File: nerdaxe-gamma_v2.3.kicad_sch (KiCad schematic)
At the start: 20 parts, among them J1 54-00164

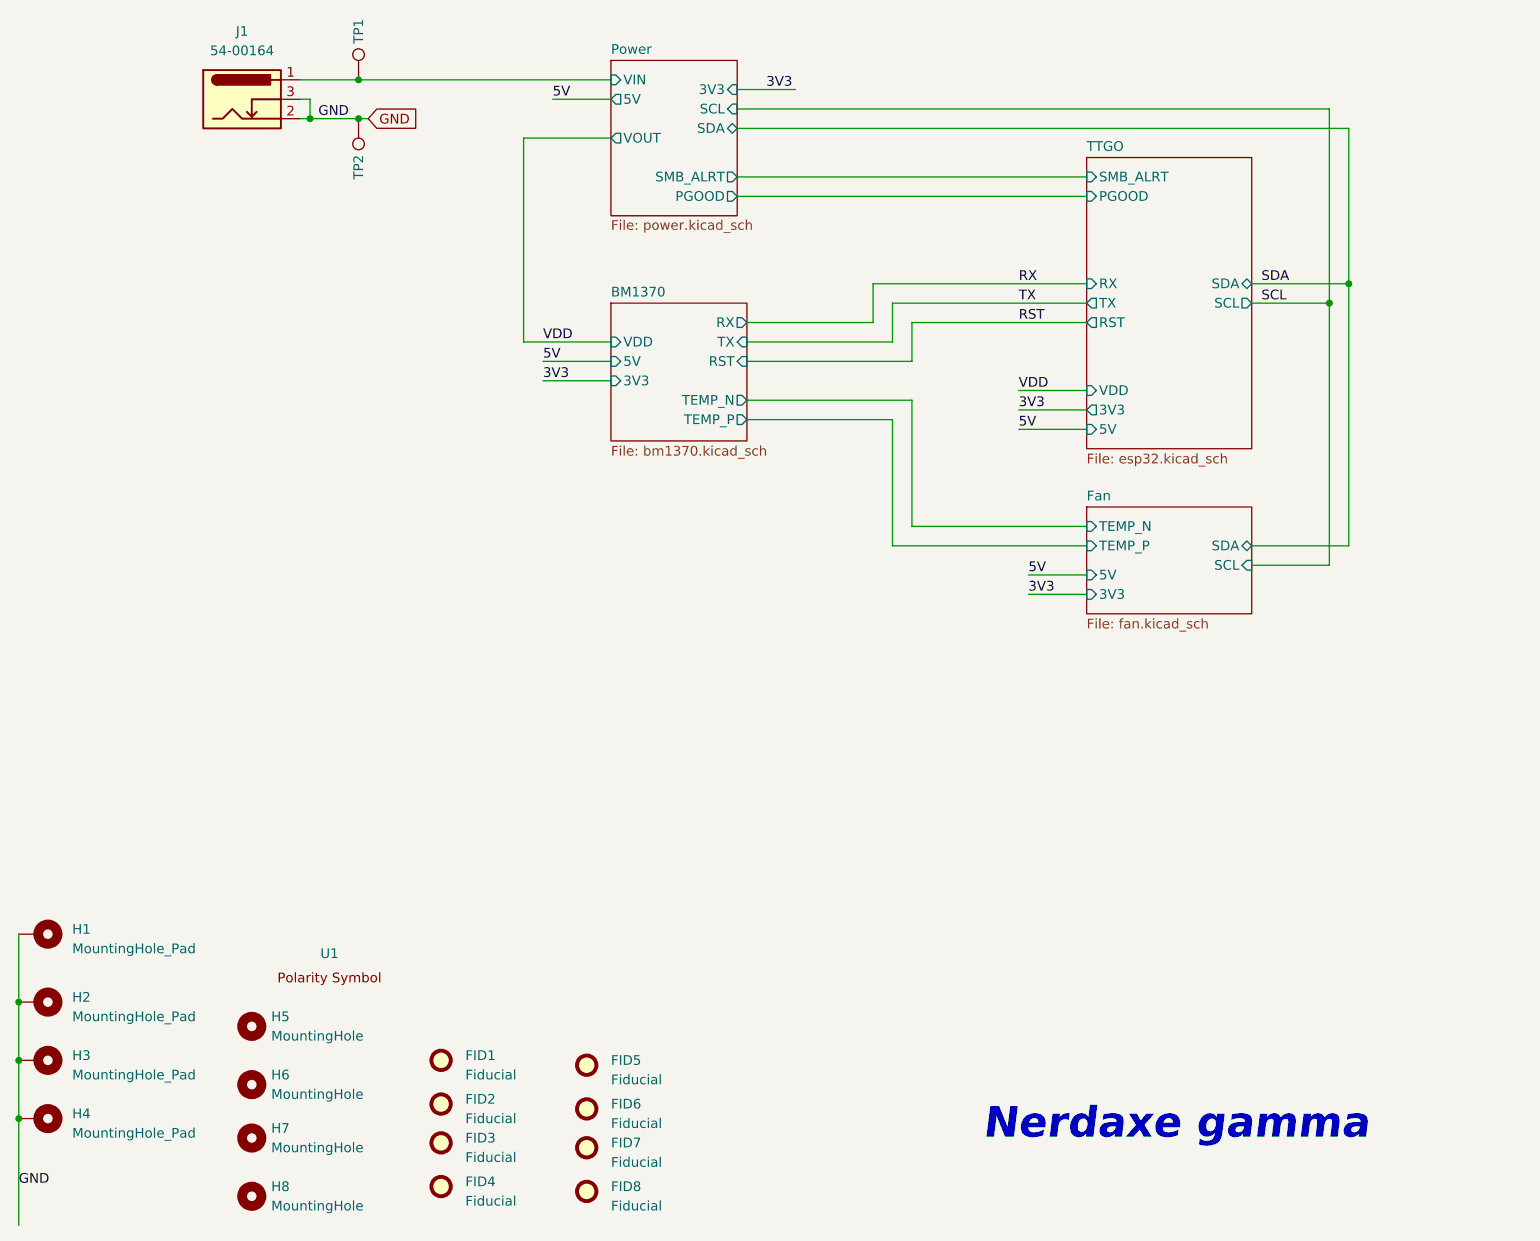
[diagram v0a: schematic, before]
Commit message: Nerdaxe Gamma v2.3
- Fix Emi CE needs
- Added ferrite beads + EMI blocking capacitors
- New components added: R16, R20, R26, R27C21, C22, C23, FB1, FB2, FB3, FB4, FB5, FB6
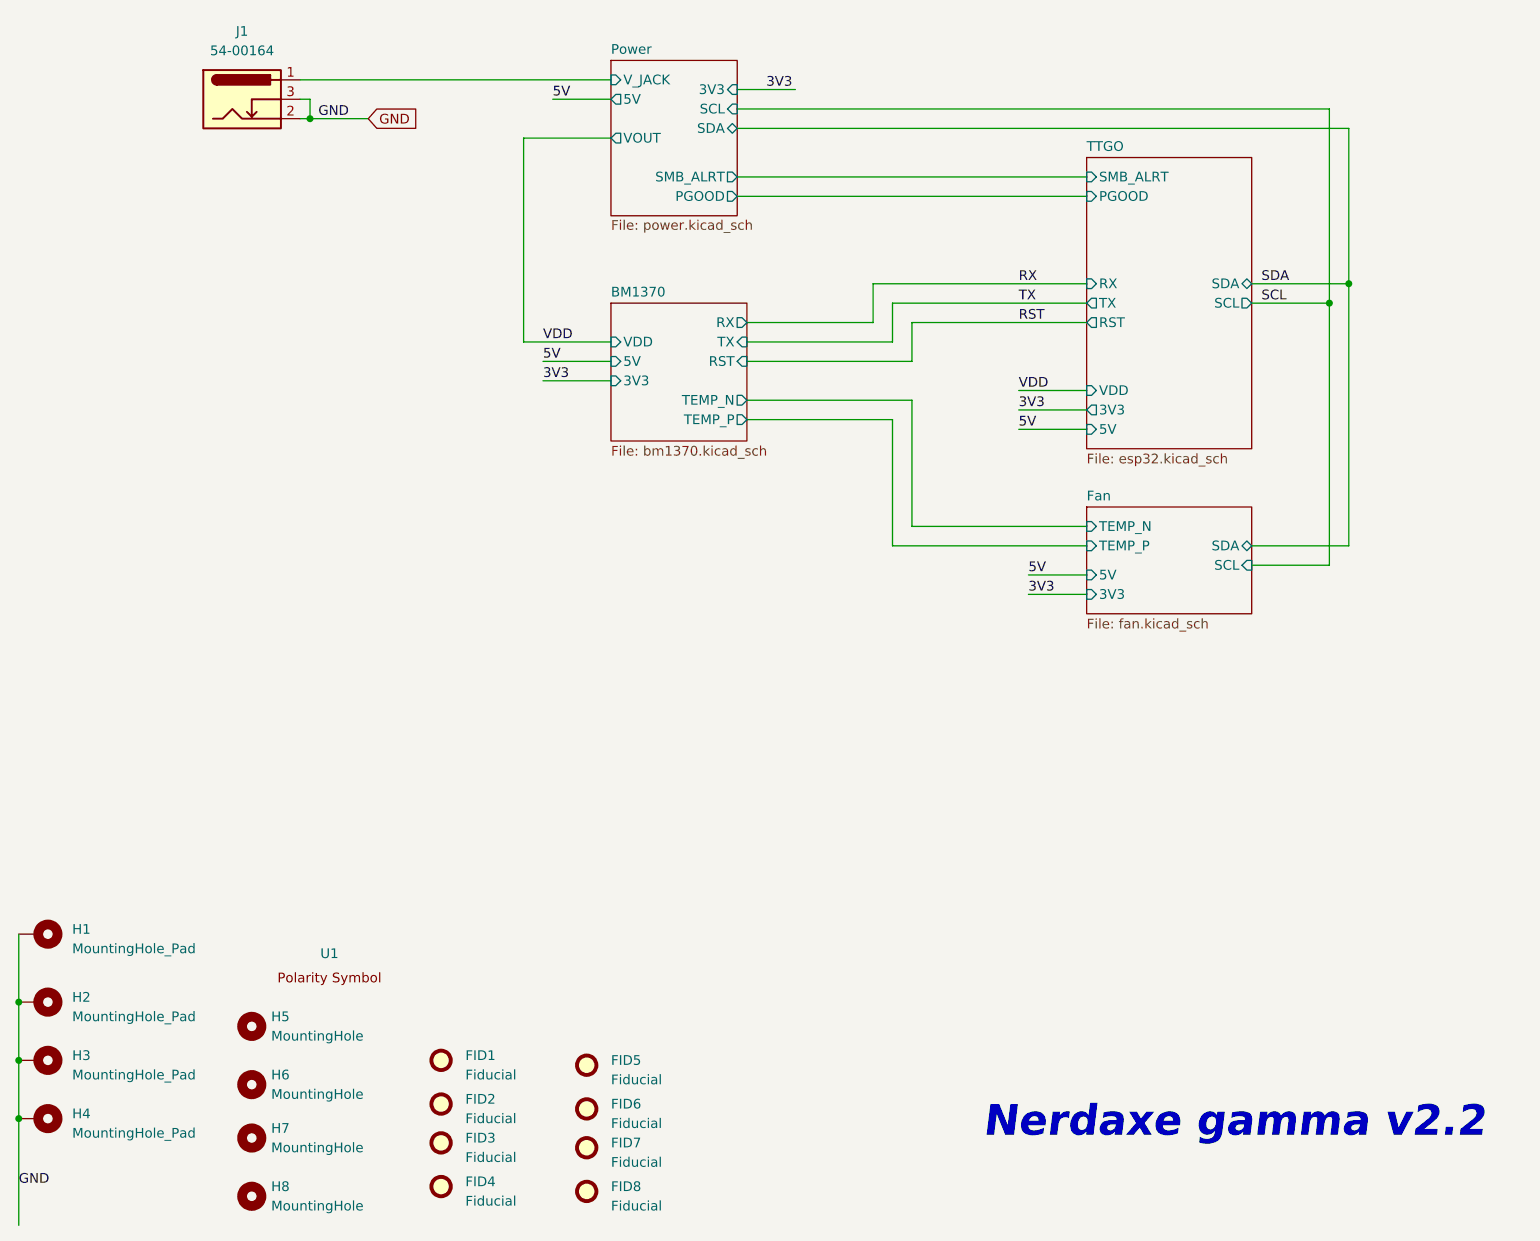
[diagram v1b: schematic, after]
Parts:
- removed TP1, TP2: TestPoint, TestPoint:TestPoint_Pad_D1.5mm, symbol Connector:TestPoint
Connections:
- net Power/VIN renamed Power/V_JACK
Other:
- sheet Power ports: added V_JACK; removed VIN
- note added: "Nerdaxe gamma v2.2"
- note removed: "Nerdaxe gamma"
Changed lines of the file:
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@@
 		(title "NerdaxeGamma")
 		(date "2024-08-16")
-		(rev "rev1")
+		(rev "rev2.2")
 	)
 	(junction
@@
 	)
 	(junction
-		(at 80.01 43.18)
-		(diameter 0)
-		(color 0 0 0 0)
-	)
-	(junction
 		(at 35.56 171.45)
 		(diameter 0)
@@
 	)
 	(junction
-		(at 80.01 48.26)
-		(diameter 0)
-		(color 0 0 0 0)
-	)
-	(junction
 		(at 35.56 163.83)
 		(diameter 0)
@@
 	(wire
 		(pts
-			(xy 80.01 48.26) (xy 81.28 48.26)
-		)
-		(stroke
-			(width 0)
-			(type default)
-		)
-	)
-	(wire
-		(pts
 			(xy 105.41 45.72) (xy 113.03 45.72)
 		)
@@
 	(wire
 		(pts
-			(xy 72.39 43.18) (xy 80.01 43.18)
+			(xy 72.39 43.18) (xy 113.03 43.18)
 		)
 		(stroke
@@
 	(wire
 		(pts
-			(xy 73.66 48.26) (xy 80.01 48.26)
+			(xy 73.66 48.26) (xy 81.28 48.26)
 		)
 		(stroke
@@
 	(wire
 		(pts
-			(xy 80.01 43.18) (xy 113.03 43.18)
-		)
-		(stroke
-			(width 0)
-			(type default)
-		)
-	)
-	(wire
-		(pts
 			(xy 149.86 104.14) (xy 149.86 87.63)
 		)
@@
 		)
 	)
-	(text "Nerdaxe gamma"
+	(text "Nerdaxe gamma v2.2"
 		(exclude_from_sim no)
-		(at 186.944 179.832 0)
+		(at 194.564 179.578 0)
 		(effects
 			(font
@@
 	)
 	(symbol
-		(lib_id "Connector:TestPoint")
-		(at 80.01 43.18 0)
-		(unit 1)
-		(exclude_from_sim no)
-		(in_bom no)
-		(on_board yes)
-		(dnp no)
-		(property "Reference" "TP1"
-			(at 80.01 36.83 90)
-			(effects
-				(font
-					(size 1.27 1.27)
-				)
-			)
-		)
-		(property "Value" "TestPoint"
-			(at 81.2799 37.465 90)
-			(effects
-				(font
-					(size 1.27 1.27)
-				)
-				(justify left)
-				(hide yes)
-			)
-		)
-		(property "Footprint" "TestPoint:TestPoint_Pad_D1.5mm"
-			(at 85.09 43.18 0)
-			(effects
-				(font
-					(size 1.27 1.27)
-				)
-				(hide yes)
-			)
-		)
-		(property "Datasheet" "~"
-			(at 85.09 43.18 0)
-			(effects
-				(font
-					(size 1.27 1.27)
-				)
-				(hide yes)
-			)
-		)
-		(property "Description" ""
-			(at 80.01 43.18 0)
-			(effects
-				(font
-					(size 1.27 1.27)
-				)
-				(hide yes)
-			)
-		)
-		(pin "1"
-		)
-		(instances
-			(project "bitaxeGamma"
-				(path "/e63e39d7-6ac0-4ffd-8aa3-1841a4541b55"
-					(reference "TP1")
-					(unit 1)
-				)
-			)
-		)
-	)
-	(symbol
-		(lib_id "Connector:TestPoint")
-		(at 80.01 48.26 180)
-		(unit 1)
-		(exclude_from_sim no)
-		(in_bom no)
-		(on_board yes)
-		(dnp no)
-		(property "Reference" "TP2"
-			(at 80.01 54.61 90)
-			(effects
-				(font
-					(size 1.27 1.27)
-				)
-			)
-		)
-		(property "Value" "TestPoint"
-			(at 78.7401 53.975 90)
-			(effects
-				(font
-					(size 1.27 1.27)
-				)
-				(justify left)
-				(hide yes)
-			)
-		)
-		(property "Footprint" "TestPoint:TestPoint_Pad_D1.5mm"
-			(at 74.93 48.26 0)
-			(effects
-				(font
-					(size 1.27 1.27)
-				)
-				(hide yes)
-			)
-		)
-		(property "Datasheet" "~"
-			(at 74.93 48.26 0)
-			(effects
-				(font
-					(size 1.27 1.27)
-				)
-				(hide yes)
-			)
-		)
-		(property "Description" ""
-			(at 80.01 48.26 0)
-			(effects
-				(font
-					(size 1.27 1.27)
-				)
-				(hide yes)
-			)
-		)
-		(pin "1"
-		)
-		(instances
-			(project "bitaxeGamma"
-				(path "/e63e39d7-6ac0-4ffd-8aa3-1841a4541b55"
-					(reference "TP2")
-					(unit 1)
-				)
-			)
-		)
-	)
-	(symbol
 		(lib_id "Mechanical:MountingHole")
 		(at 66.04 189.23 0)
@@
 		)
 		(instances
-			(project "nerdaxe-gamma"
+			(project "nerdaxe-gamma_v2.2"
 				(path "/e63e39d7-6ac0-4ffd-8aa3-1841a4541b55"
 					(page "4")
@@
 		)
 		(instances
-			(project "nerdaxe-gamma"
+			(project "nerdaxe-gamma_v2.2"
 				(path "/e63e39d7-6ac0-4ffd-8aa3-1841a4541b55"
 					(page "5")
@@
 			)
 		)
-		(pin "VIN" input
+		(pin "V_JACK" input
 			(at 113.03 43.18 180)
 			(effects
@@
 		)
 		(instances
-			(project "nerdaxe-gamma"
+			(project "nerdaxe-gamma_v2.2"
 				(path "/e63e39d7-6ac0-4ffd-8aa3-1841a4541b55"
 					(page "2")
@@
 		)
 		(instances
-			(project "nerdaxe-gamma"
+			(project "nerdaxe-gamma_v2.2"
 				(path "/e63e39d7-6ac0-4ffd-8aa3-1841a4541b55"
 					(page "3")
